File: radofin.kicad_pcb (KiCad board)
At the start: 2 copper layers, 68 x 68 mm, 6 parts, among them J1 Conn_02x16_Counter_Clockwise, SW2 SW_DIP_x03, U1 27C128

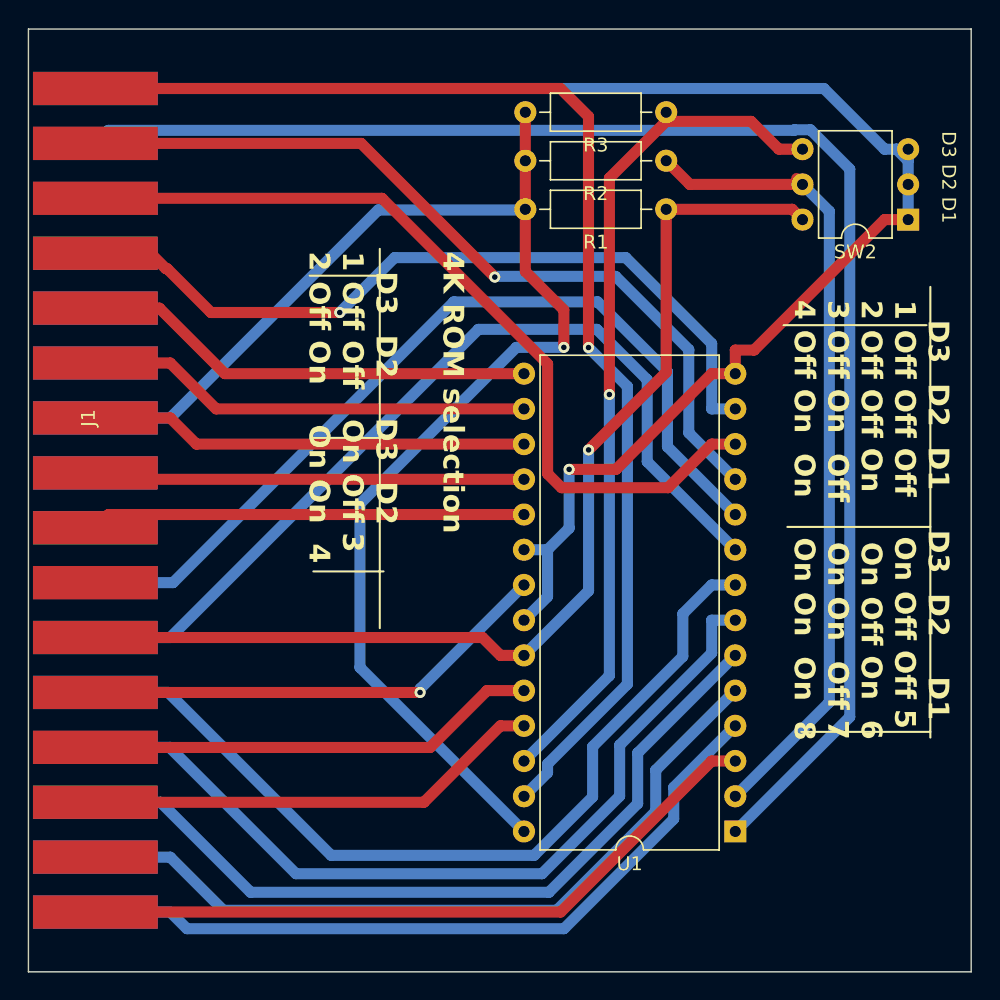
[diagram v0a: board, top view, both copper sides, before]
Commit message: Rewiring after an optical review
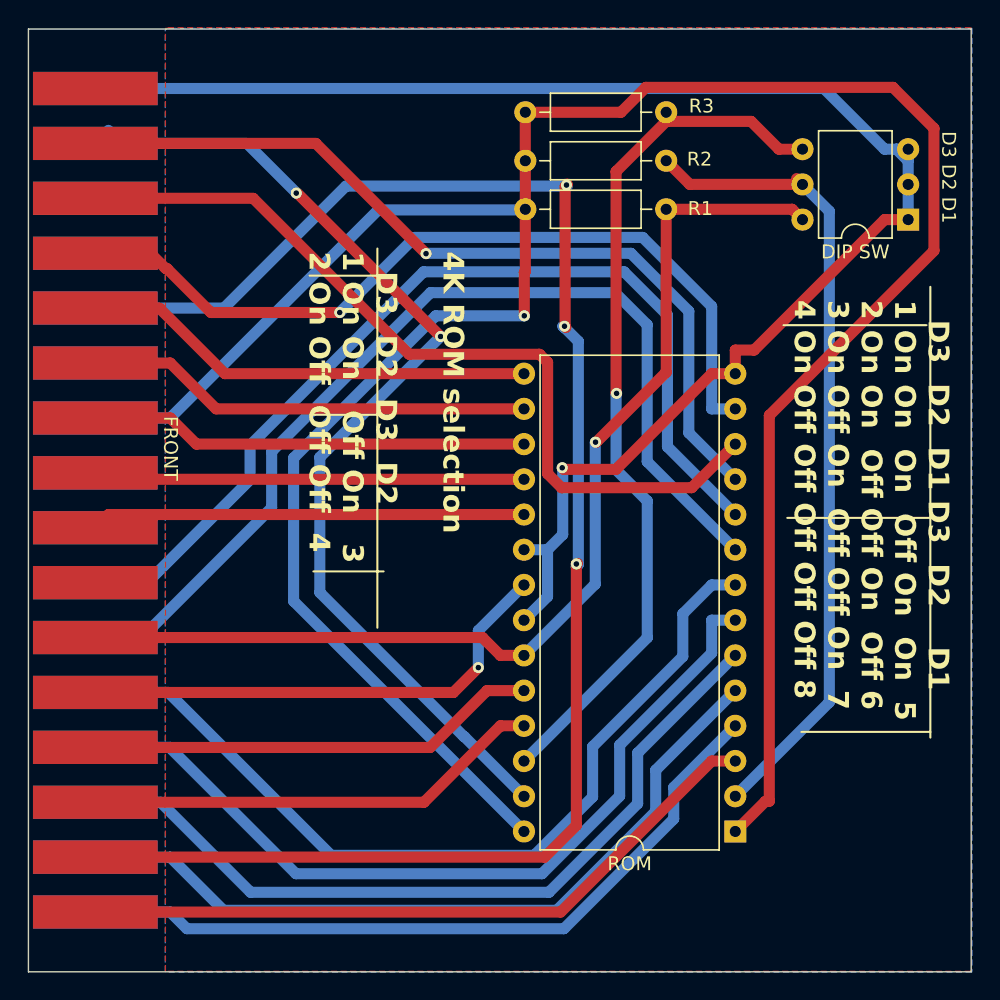
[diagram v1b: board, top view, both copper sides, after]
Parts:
- DIP SW: renamed from SW2
- renumbered J1 to FRONT, U1 to ROM
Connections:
- FRONT pad 16: //PGM -> unconnected-(J1-Pin_16-Pad16)
- FRONT pad 18: /VPP -> //PGM
- FRONT pad 2: unconnected-(J1-Pin_2-Pad2) -> Net-(J1-Pin_2)
- FRONT pad 21: unconnected-(J1-Pin_21-Pad21) -> Net-(J1-Pin_2)
- ROM pad 1: /VPP -> VCC
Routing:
- net Net-(J1-Pin_2): track 0.00 -> 120.9 mm, vias 0 -> 3
- net /VPP: track 107.2 -> 0.00 mm
- net VCC: track 103.3 -> 194.9 mm
- net //PGM: track 89.7 -> 74.9 mm, vias 1 -> 2
- net /A1: track 65.4 -> 72.3 mm
- net /A0: track 64.1 -> 69.7 mm
- net /D2: track 56.8 -> 59.6 mm
- net /A13: track 61.9 -> 63.8 mm
- net /D0: track 59.7 -> 61.3 mm
- net /A10: track 34.3 -> 35.7 mm
- added copper zone on B.Cu, net GND
- added copper zone on F.Cu, net VCC
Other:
- board text added: "4K ROM selection D3 D2 D3 D2 1 On On Off On 3 2 On Off Off Off 4"
- board text added: "D3 D2 D1 D3 D2 D1 1 On On On Off On On 5 2 On On Off Off On Off 6 3 On Off On Off Off On 7 4 On Off Off Off Off Off 8"
- board text removed: "4K ROM selection D3 D2 D3 D2 1 Off Off On Off 3 2 Off On On On 4"
- board text removed: "D3 D2 D1 D3 D2 D1 1 Off Off Off On Off Off 5 2 Off Off On On Off On 6 3 Off On Off On On Off 7 4 Off On On On On On 8"
